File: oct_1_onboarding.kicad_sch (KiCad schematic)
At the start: 52 parts

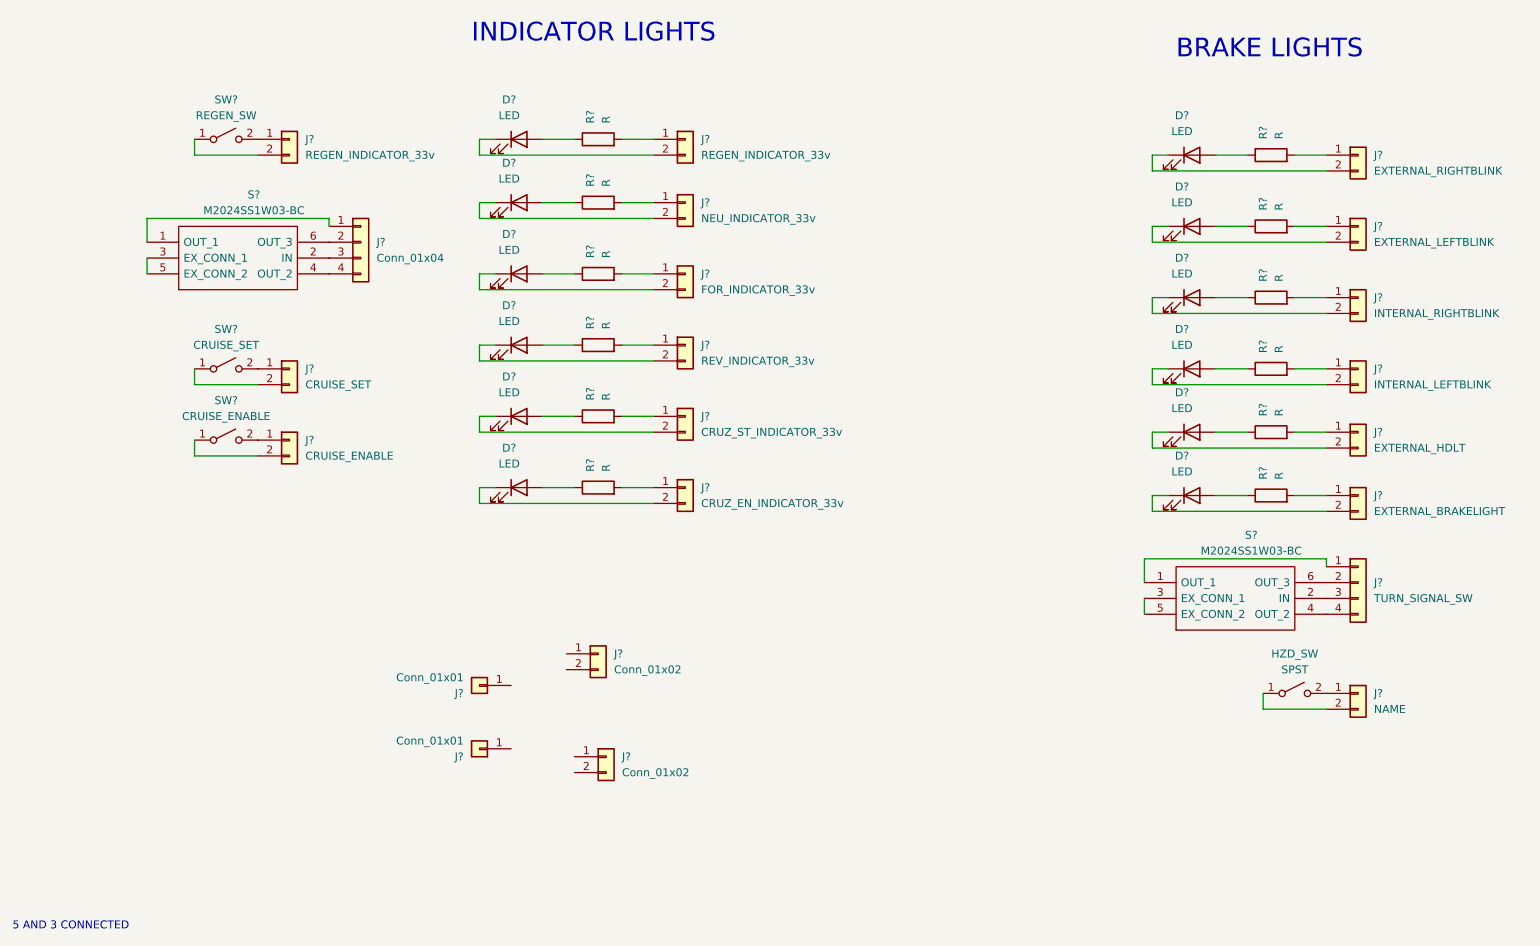
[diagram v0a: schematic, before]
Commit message: completed schematic and footprint
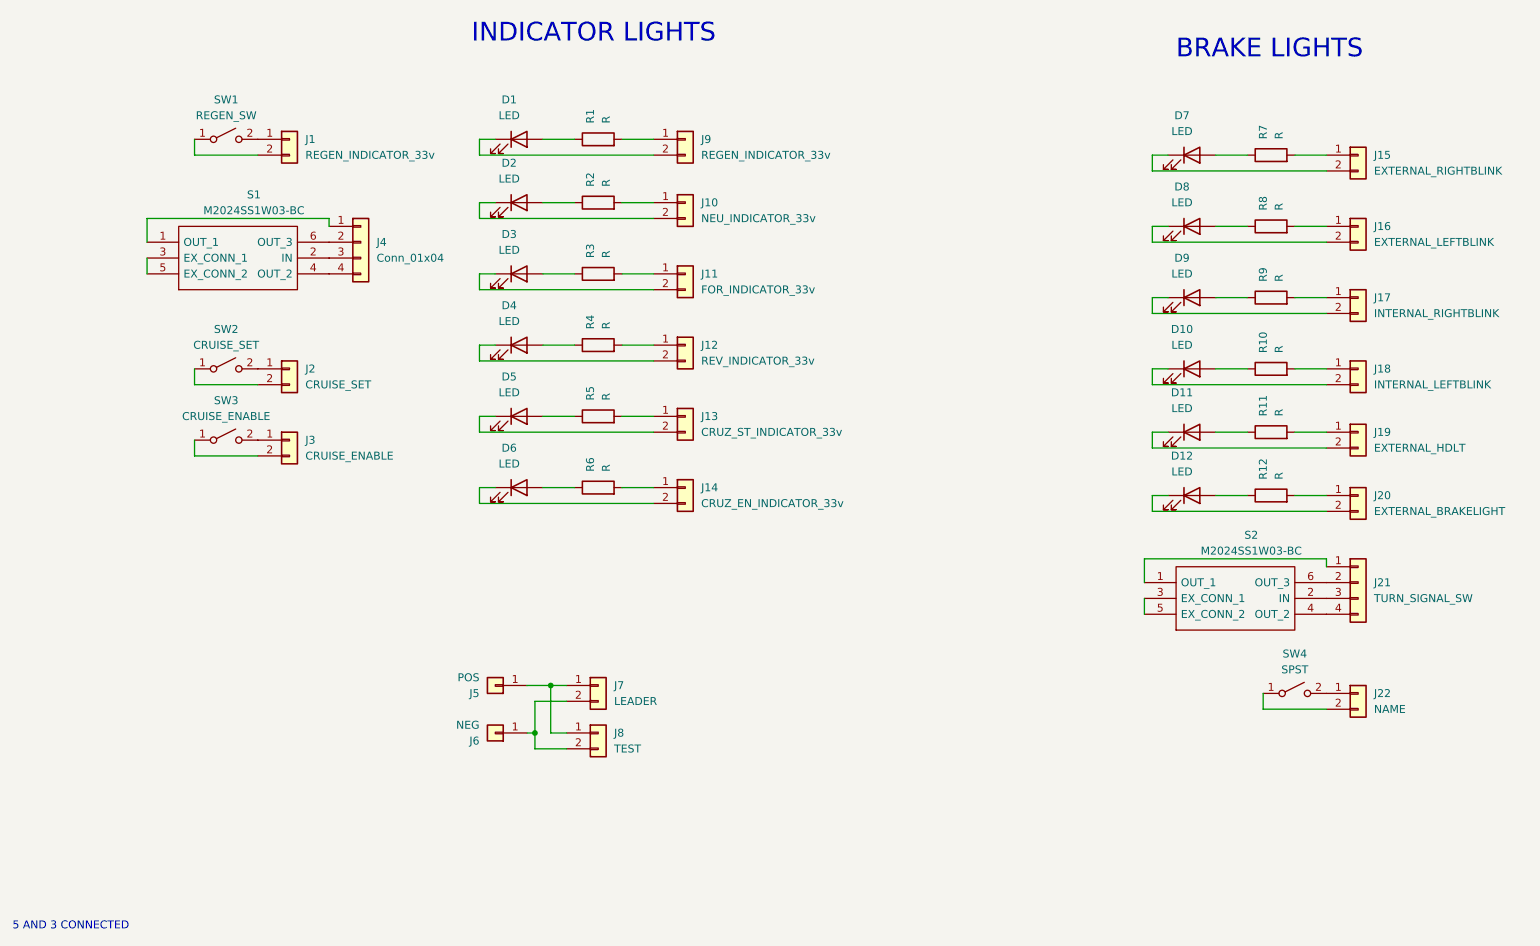
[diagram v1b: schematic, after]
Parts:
- D1, D10, D11, D12, D2, D3, D4, D5, D6, D7, D8, D9: renamed from D?; footprint (none) -> LED_SMD:LED_0805_2012Metric
- J1: renamed from J?; footprint (none) -> Connector_Molex:Molex_Micro-Fit_3.0_43045-1000_2x05_P3.00mm_Horizontal
- J10, J11, J12, J13, J14, J15, J16, J17, J18, J19, J2, J20, J22, J3, J9: renamed from J?; footprint (none) -> Connector_Molex:Molex_Micro-Fit_3.0_43650-0210_1x02-1MP_P3.00mm_Horizontal
- J21, J4: renamed from J?; footprint (none) -> Connector_Molex:Molex_Micro-Fit_3.0_43650-0400_1x04_P3.00mm_Horizontal
- J5: renamed from J?; value Conn_01x01 -> POS; footprint (none) -> UTSVT_Connectors:Banana_Jack_1_Pin_4mm
- J6: renamed from J?; value Conn_01x01 -> NEG; footprint (none) -> UTSVT_Connectors:Banana_Jack_1_Pin_4mm
- J7: renamed from J?; value Conn_01x02 -> LEADER; footprint (none) -> Connector_Molex:Molex_Micro-Fit_3.0_43650-0210_1x02-1MP_P3.00mm_Horizontal
- J8: renamed from J?; value Conn_01x02 -> TEST; footprint (none) -> Connector_Molex:Molex_Micro-Fit_3.0_43650-0210_1x02-1MP_P3.00mm_Horizontal
- R1, R10, R11, R12, R2, R3, R4, R5, R6, R7, R8, R9: renamed from R?; footprint (none) -> Resistor_SMD:R_0805_2012Metric
- S1, S2: renamed from S?; footprint M2024SS1W03BC -> UTSVT_Special:M2024SS1W03BC
- SW1: renamed from SW?; footprint (none) -> Connector_Molex:Molex_Micro-Fit_3.0_43650-0400_1x04_P3.00mm_Horizontal
- SW2, SW3: renamed from SW?; footprint (none) -> UTSVT_Special:2MS6T1B3M2QES
- SW4: renamed from HZD_SW; footprint (none) -> UTSVT_Special:2MS6T1B3M2QES
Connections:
- net at J5.1 (Pin_1): now also J7.1 (Pin_1), J8.1 (Pin_1)
- net at J7.2 (Pin_2): now also J6.1 (Pin_1), J8.2 (Pin_2)
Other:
- moved on the sheet: J5, J6, J7, J8

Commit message: completed schematic and pcb ish
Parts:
- added H1, H2, H3, H4: MountingHole, MountingHole:MountingHole_3mm, symbol Mechanical:MountingHole
- added LOGO1: Dr. Hallock Logo, UTSVT_Special:Hallock_Image_Tiny, symbol Controls-LightingPCB-rescue:Logo_Placeholder-utsvt-misc
- added LOGO2: UTSVT Logo, UTSVT_Special:UTSVT_Logo_Symbol, symbol Controls-LightingPCB-rescue:Logo_Placeholder-utsvt-misc
- J1: value REGEN_INDICATOR_33v -> REGEN_IND_33v; footprint Connector_Molex:Molex_Micro-Fit_3.0_43045-1000_2x05_P3.00mm_Horizontal -> Connector_Molex:Molex_Micro-Fit_3.0_43650-0200_1x02_P3.00mm_Horizontal
- J10: value NEU_INDICATOR_33v -> NEU_IND_33v; footprint Connector_Molex:Molex_Micro-Fit_3.0_43650-0210_1x02-1MP_P3.00mm_Horizontal -> Connector_Molex:Molex_Micro-Fit_3.0_43650-0200_1x02_P3.00mm_Horizontal
- J11: value FOR_INDICATOR_33v -> FOR_IND_33v; footprint Connector_Molex:Molex_Micro-Fit_3.0_43650-0210_1x02-1MP_P3.00mm_Horizontal -> Connector_Molex:Molex_Micro-Fit_3.0_43650-0200_1x02_P3.00mm_Horizontal
- J12: value REV_INDICATOR_33v -> REV_IND_33v; footprint Connector_Molex:Molex_Micro-Fit_3.0_43650-0210_1x02-1MP_P3.00mm_Horizontal -> Connector_Molex:Molex_Micro-Fit_3.0_43650-0200_1x02_P3.00mm_Horizontal
- J13: value CRUZ_ST_INDICATOR_33v -> CRUZ_ST; footprint Connector_Molex:Molex_Micro-Fit_3.0_43650-0210_1x02-1MP_P3.00mm_Horizontal -> Connector_Molex:Molex_Micro-Fit_3.0_43650-0200_1x02_P3.00mm_Horizontal
- J14: value CRUZ_EN_INDICATOR_33v -> CRUZ_EN; footprint Connector_Molex:Molex_Micro-Fit_3.0_43650-0210_1x02-1MP_P3.00mm_Horizontal -> Connector_Molex:Molex_Micro-Fit_3.0_43650-0200_1x02_P3.00mm_Horizontal
- J15: value EXTERNAL_RIGHTBLINK -> EXT_RBLINK; footprint Connector_Molex:Molex_Micro-Fit_3.0_43650-0210_1x02-1MP_P3.00mm_Horizontal -> Connector_Molex:Molex_Micro-Fit_3.0_43650-0200_1x02_P3.00mm_Horizontal
- J16: value EXTERNAL_LEFTBLINK -> EXT_LBLINK; footprint Connector_Molex:Molex_Micro-Fit_3.0_43650-0210_1x02-1MP_P3.00mm_Horizontal -> Connector_Molex:Molex_Micro-Fit_3.0_43650-0200_1x02_P3.00mm_Horizontal
- J17: value INTERNAL_RIGHTBLINK -> INT_RBLINK; footprint Connector_Molex:Molex_Micro-Fit_3.0_43650-0210_1x02-1MP_P3.00mm_Horizontal -> Connector_Molex:Molex_Micro-Fit_3.0_43650-0200_1x02_P3.00mm_Horizontal
- J18: value INTERNAL_LEFTBLINK -> INT_LBLINK; footprint Connector_Molex:Molex_Micro-Fit_3.0_43650-0210_1x02-1MP_P3.00mm_Horizontal -> Connector_Molex:Molex_Micro-Fit_3.0_43650-0200_1x02_P3.00mm_Horizontal
- J19: value EXTERNAL_HDLT -> EXT_HDLT; footprint Connector_Molex:Molex_Micro-Fit_3.0_43650-0210_1x02-1MP_P3.00mm_Horizontal -> Connector_Molex:Molex_Micro-Fit_3.0_43650-0200_1x02_P3.00mm_Horizontal
- J2, J22, J3, J7, J8: footprint Connector_Molex:Molex_Micro-Fit_3.0_43650-0210_1x02-1MP_P3.00mm_Horizontal -> Connector_Molex:Molex_Micro-Fit_3.0_43650-0200_1x02_P3.00mm_Horizontal
- J20: value EXTERNAL_BRAKELIGHT -> EXT_BLIGHT; footprint Connector_Molex:Molex_Micro-Fit_3.0_43650-0210_1x02-1MP_P3.00mm_Horizontal -> Connector_Molex:Molex_Micro-Fit_3.0_43650-0200_1x02_P3.00mm_Horizontal
- J9: value REGEN_INDICATOR_33v -> REGEN_IND_33v; footprint Connector_Molex:Molex_Micro-Fit_3.0_43650-0210_1x02-1MP_P3.00mm_Horizontal -> Connector_Molex:Molex_Micro-Fit_3.0_43650-0200_1x02_P3.00mm_Horizontal
- SW1: footprint Connector_Molex:Molex_Micro-Fit_3.0_43650-0400_1x04_P3.00mm_Horizontal -> UTSVT_Special:2MS6T1B3M2QES
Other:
- moved on the sheet: J5, J6, J7, J8
